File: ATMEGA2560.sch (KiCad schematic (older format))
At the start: 3 parts, among them U1 ATmega2560-16AU

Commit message: added peripherals
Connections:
- net labels added: DIR_X, EN_X, P_0_I, P_1_I, P_2_I, P_3_I, STEP_X, X2_0, X2_1, X2_2, X2_3, X2_4, X2_[0..4], ~CS~_SPI_X
- wire segments 38 -> 56
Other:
- moved on the sheet: R2
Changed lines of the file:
@@
 	1    0    0    -1
 $EndComp
-Text HLabel 5800 1650 2    50   Output ~ 0
+Text HLabel 6250 1650 2    50   Output ~ 0
 ~SS_cop
 Wire Wire Line
@@
 Connection ~ 5650 1650
 Wire Wire Line
-	5650 1650 5800 1650
+	5650 1650 6250 1650
 $Comp
 L Device:R R2
 U 1 1 5EE7AE50
-P 5650 2250
-F 0 "R2" H 5720 2341 50  0000 L CNN
-F 1 "10K" H 5720 2250 50  0000 L CNN
-F 2 "" V 5580 2250 50  0001 C CNN
-F 3 "~" H 5650 2250 50  0001 C CNN
-F 4 "1%" H 5720 2159 50  0000 L CNN "Tolerance"
-	1    5650 2250
+P 6750 2250
+F 0 "R2" H 6820 2341 50  0000 L CNN
+F 1 "10K" H 6820 2250 50  0000 L CNN
+F 2 "" V 6680 2250 50  0001 C CNN
+F 3 "~" H 6750 2250 50  0001 C CNN
+F 4 "1%" H 6820 2159 50  0000 L CNN "Tolerance"
+	1    6750 2250
 	1    0    0    -1
 $EndComp
 Wire Wire Line
-	5300 2550 5650 2550
-Wire Wire Line
-	5650 2400 5650 2550
+	5300 2550 6750 2550
+Wire Wire Line
+	6750 2400 6750 2550
 Text HLabel 6000 2750 2    50   Input ~ 0
 SCK_SPI
@@
 Wire Wire Line
 	3300 5650 3700 5650
+Wire Wire Line
+	2900 900  3150 900
+Wire Wire Line
+	2900 1000 3150 1000
+Wire Wire Line
+	2900 1100 3150 1100
+Wire Wire Line
+	2900 1200 3150 1200
+Wire Wire Line
+	2900 1300 3150 1300
+Entry Wire Line
+	3150 900  3250 1000
+Entry Wire Line
+	3150 1000 3250 1100
+Entry Wire Line
+	3150 1100 3250 1200
+Entry Wire Line
+	3150 1200 3250 1300
+Entry Wire Line
+	3150 1300 3250 1400
+Text HLabel 3350 600  2    79   Input ~ 0
+X2_[0..4]
+Wire Bus Line
+	3250 600  3350 600
+Text Label 2900 900  0    59   ~ 0
+X2_0
+Text Label 2900 1000 0    59   ~ 0
+X2_1
+Text Label 2900 1100 0    59   ~ 0
+X2_2
+Text Label 2900 1200 0    59   ~ 0
+X2_3
+Text Label 2900 1300 0    59   ~ 0
+X2_4
+Wire Wire Line
+	3450 4350 3700 4350
+Wire Wire Line
+	3450 4450 3700 4450
+Wire Wire Line
+	3450 4550 3700 4550
+Wire Wire Line
+	3450 4650 3700 4650
+Wire Wire Line
+	3450 4750 3700 4750
+Text Label 3450 4350 0    59   ~ 0
+X2_0
+Text Label 3450 4450 0    59   ~ 0
+X2_1
+Text Label 3450 4550 0    59   ~ 0
+X2_2
+Text Label 3450 4650 0    59   ~ 0
+X2_3
+Text Label 3450 4750 0    59   ~ 0
+X2_4
+Text HLabel 5500 6150 2    59   Input ~ 0
+P_0_I
+Text HLabel 5500 6250 2    59   Input ~ 0
+P_1_I
+Text HLabel 5500 6350 2    59   Input ~ 0
+P_2_I
+Text HLabel 5500 6450 2    59   Input ~ 0
+P_3_I
+Wire Wire Line
+	5300 6150 5500 6150
+Wire Wire Line
+	5300 6250 5500 6250
+Wire Wire Line
+	5300 6350 5500 6350
+Wire Wire Line
+	5300 6450 5500 6450
+Text Label 6000 2050 0    59   ~ 0
+X_1
+Text Label 6000 2150 0    59   ~ 0
+X_2
+Wire Wire Line
+	6000 2050 5300 2050
+Wire Wire Line
+	6000 2150 5300 2150
+Text Label 5750 2050 2    39   ~ 0
+STEP_X
+Text Label 5750 2150 2    39   ~ 0
+DIR_X
+Text Label 6000 1950 0    59   ~ 0
+X_3
+Wire Wire Line
+	6000 1950 5300 1950
+Text Label 5750 1950 2    39   ~ 0
+EN_X
+Text Label 6000 1850 0    59   ~ 0
+X_0
+Wire Wire Line
+	6000 1850 5300 1850
+Text Label 5750 1850 2    39   ~ 0
+~CS~_SPI_X
 Wire Bus Line
 	1000 550  1000 1500
@@
 Wire Bus Line
 	2350 550  2350 1500
+Wire Bus Line
+	3250 600  3250 1550
 $EndSCHEMATC

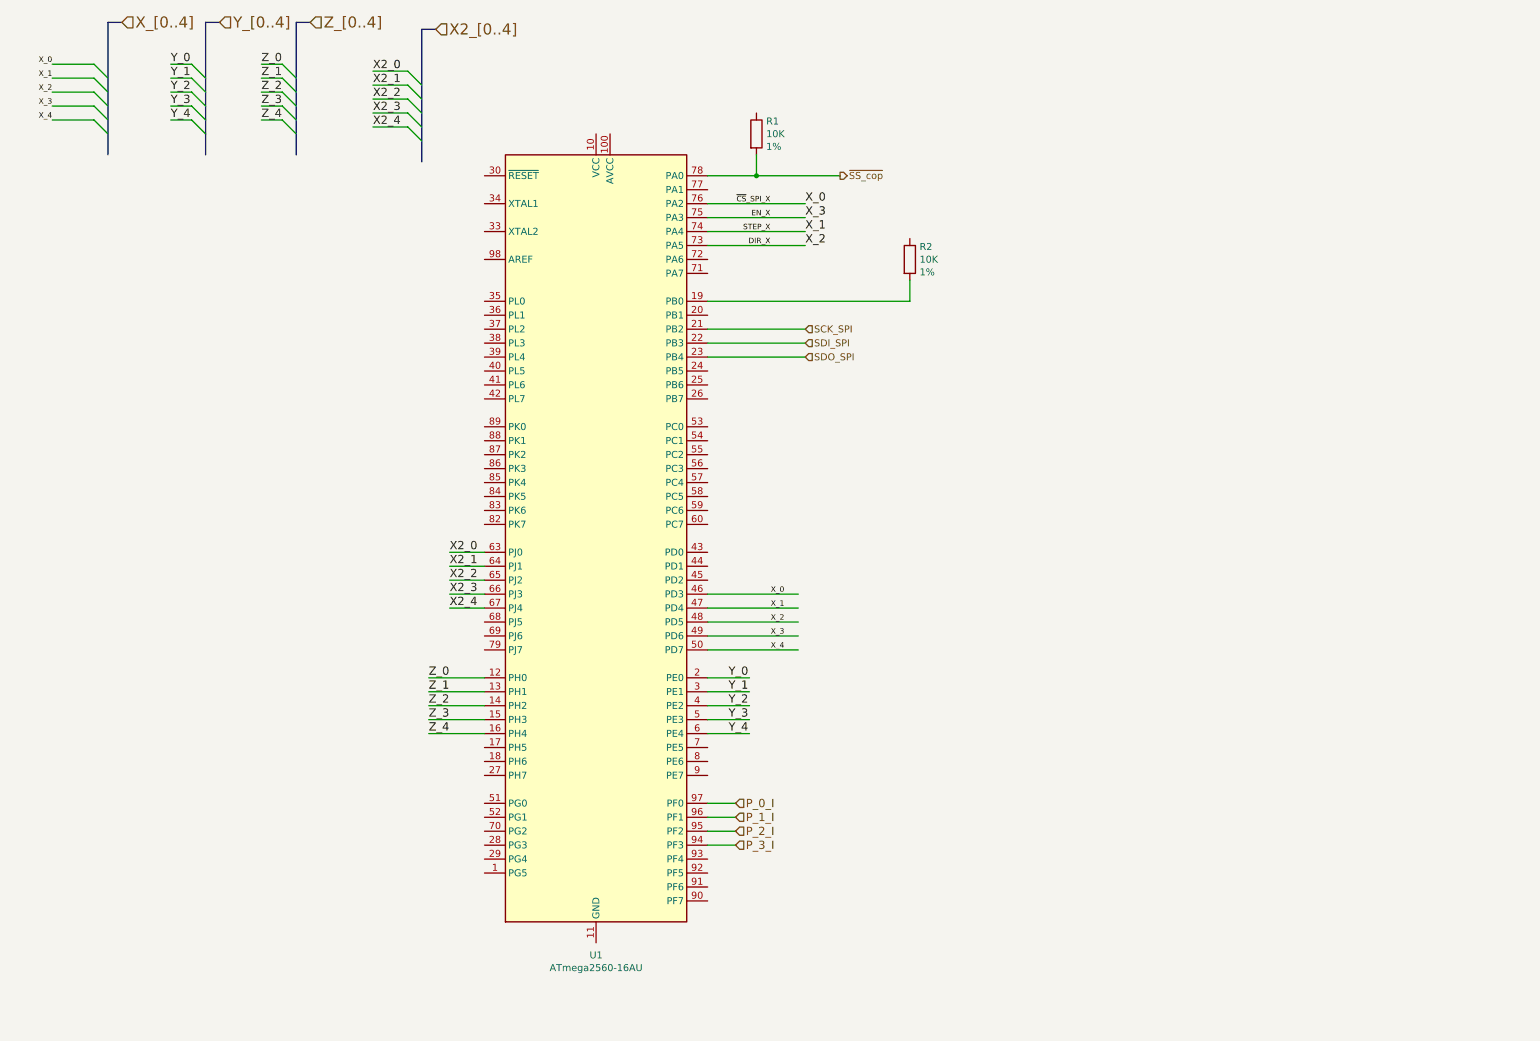
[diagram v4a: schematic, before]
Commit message: added RESET and XTAL to atmega2560
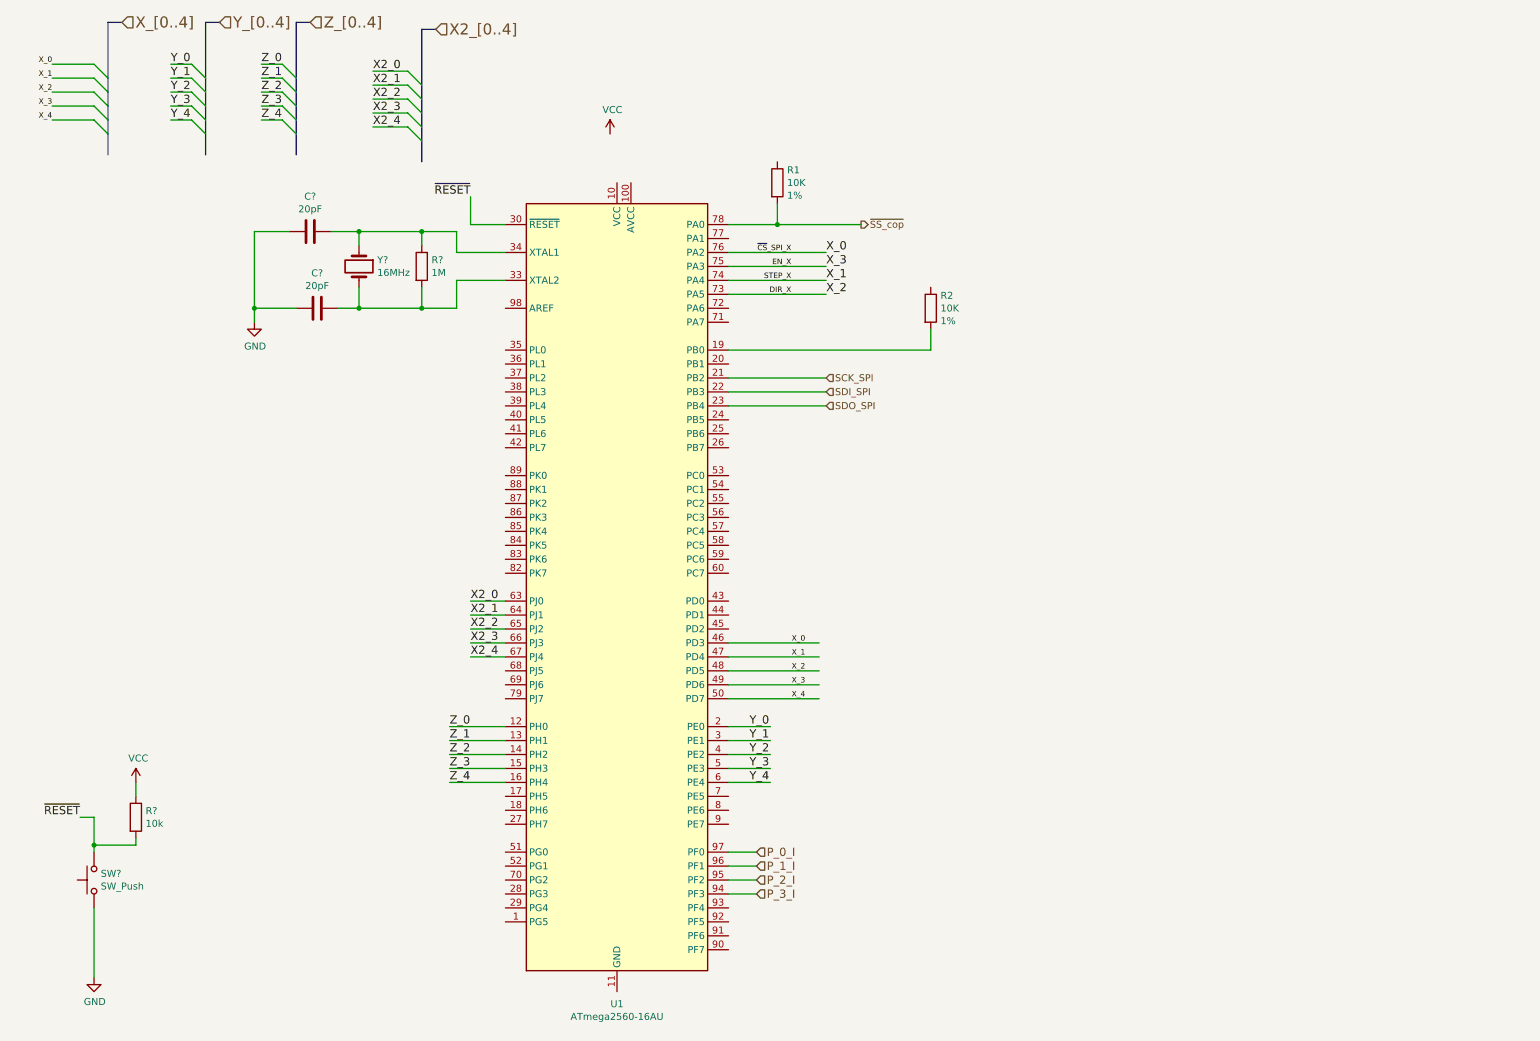
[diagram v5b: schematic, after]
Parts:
- added C? (x2): 20pF, Capacitors_SMD:C_0603_HandSoldering, symbol Device:C
- added R?: 1M, Resistors_SMD:R_0805_HandSoldering, symbol Device:R
- added R?: 10k, Resistors_SMD:R_0603_HandSoldering, symbol Device:R
- added SW?: SW_Push, symbol Switch:SW_Push
- added Y?: 16MHz, Crystals:Crystal_HC49-4H_Vertical, symbol Device:Crystal
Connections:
- net labels added: GND, VCC, ~RESET
- wire segments 56 -> 83
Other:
- moved on the sheet: R1, R2, U1

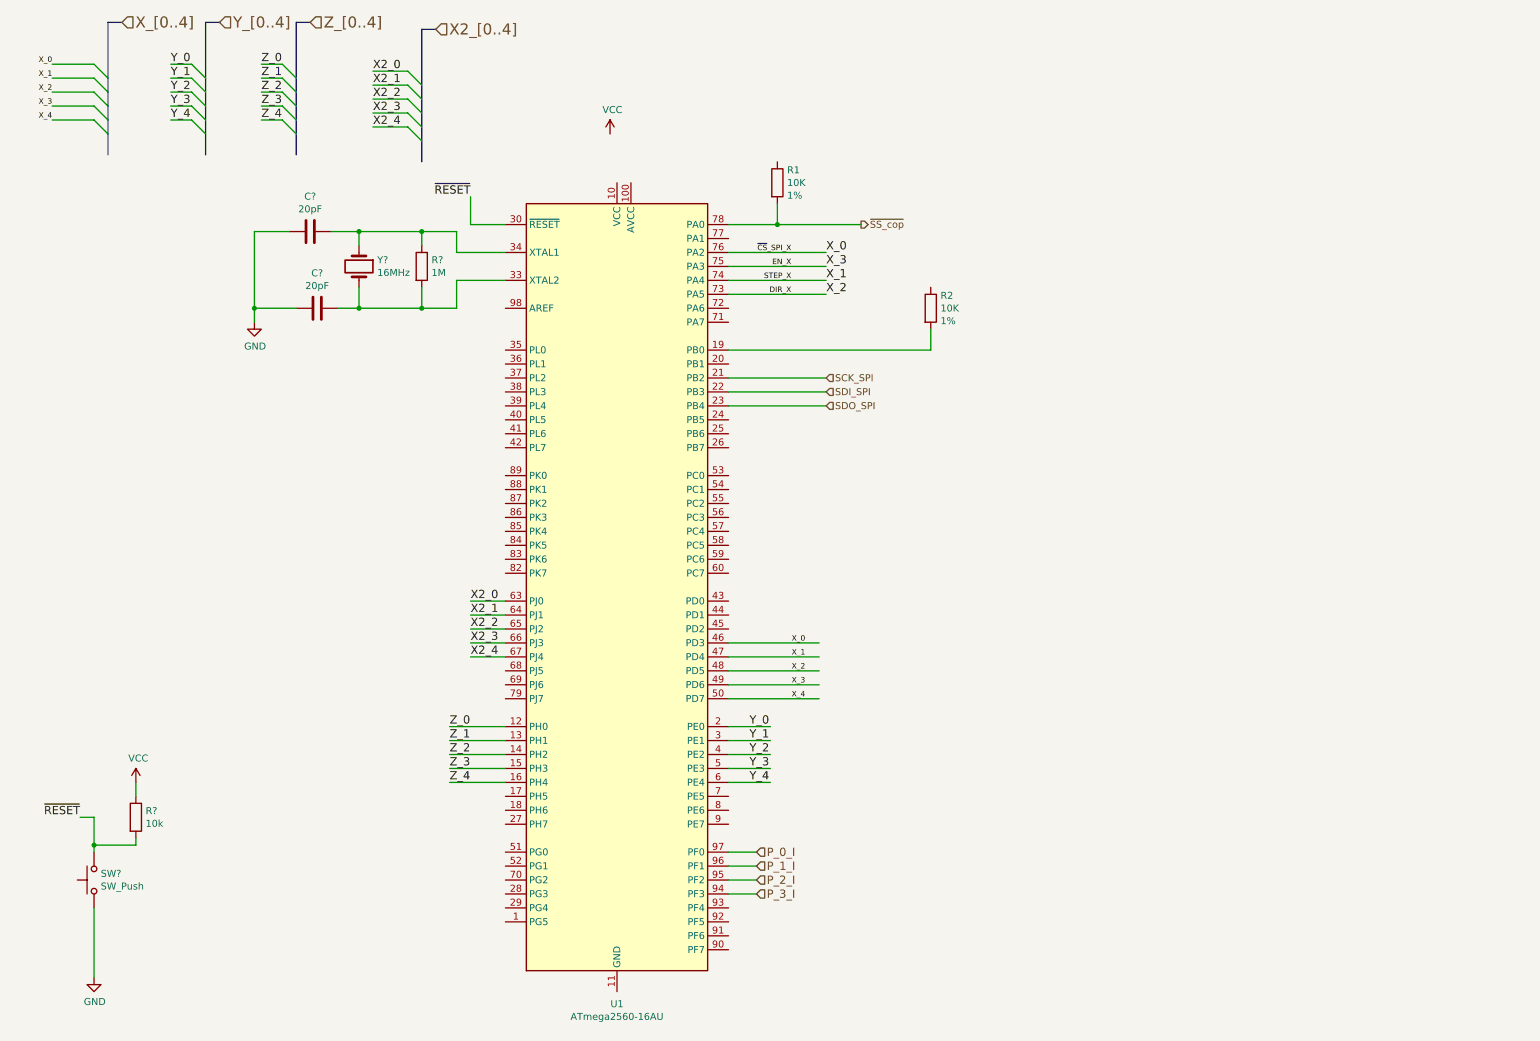
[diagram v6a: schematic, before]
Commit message: updated ATMEGA and regulators
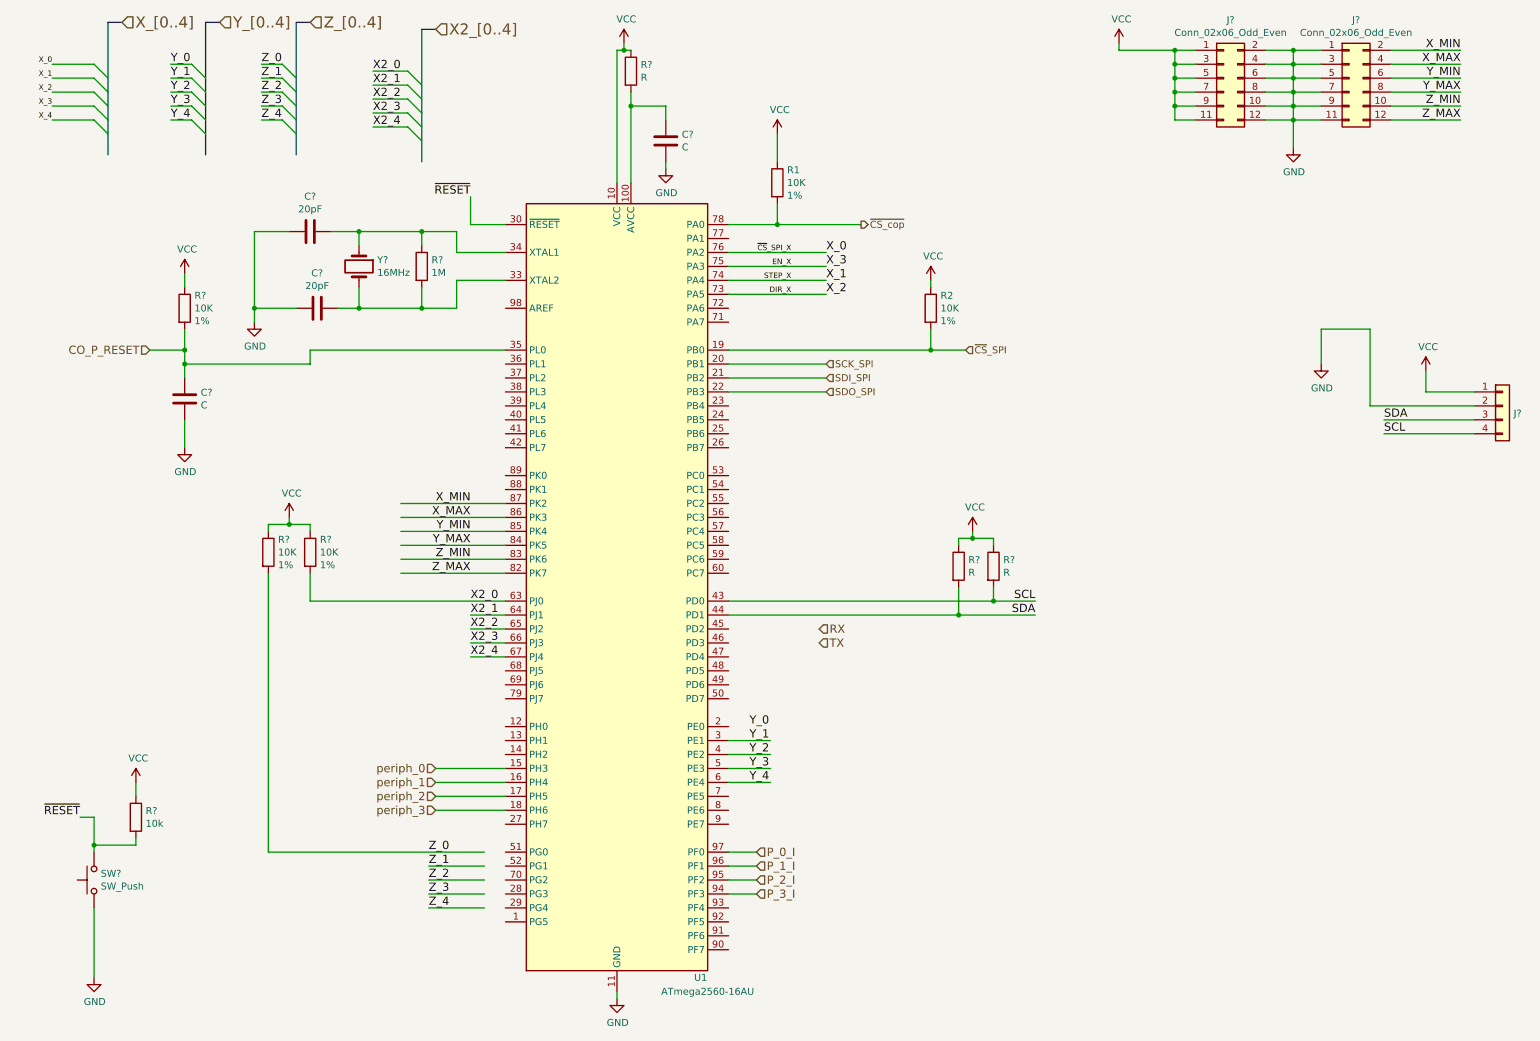
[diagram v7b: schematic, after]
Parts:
- added C? (x2): C, symbol Device:C
- added J? (x2): Conn_02x06_Odd_Even, symbol Connector_Generic:Conn_02x06_Odd_Even
- added J?: Conn_01x04, symbol Connector_Generic:Conn_01x04
- added R? (x3): R, symbol Device:R
- added R? (x3): 10K, symbol Device:R
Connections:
- net labels added: CO_P_RESET, RX, SCL, SDA, TX, X_MAX, X_MIN, Y_MAX, Y_MIN, Z_MAX, Z_MIN, periph_0, periph_1, periph_2, periph_3, ~CS_cop, ~CS~_SPI
- net labels removed: ~SS_cop
- wire segments 83 -> 172
